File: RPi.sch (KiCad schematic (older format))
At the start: 8 parts, among them U3 LMS6002DR2, U4 ECP5, X3 RaspberryPiConnector

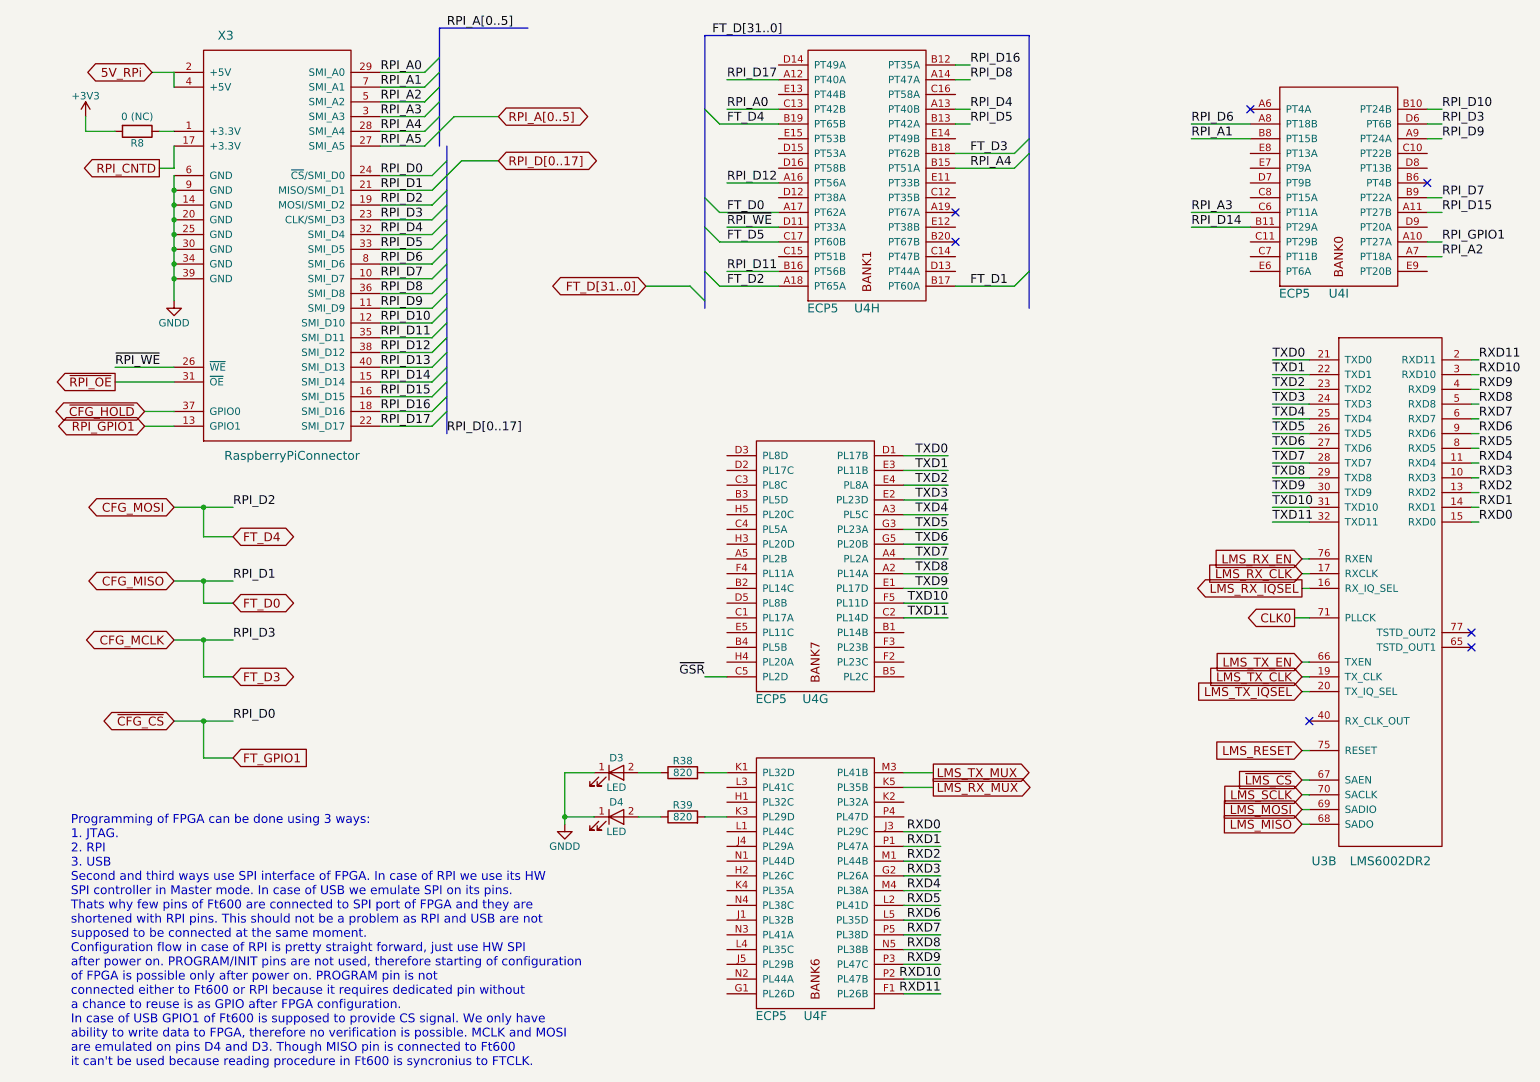
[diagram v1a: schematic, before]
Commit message: Start tracing IO Fix connector for Rpi Use LED indicator for TX/RX LEDs
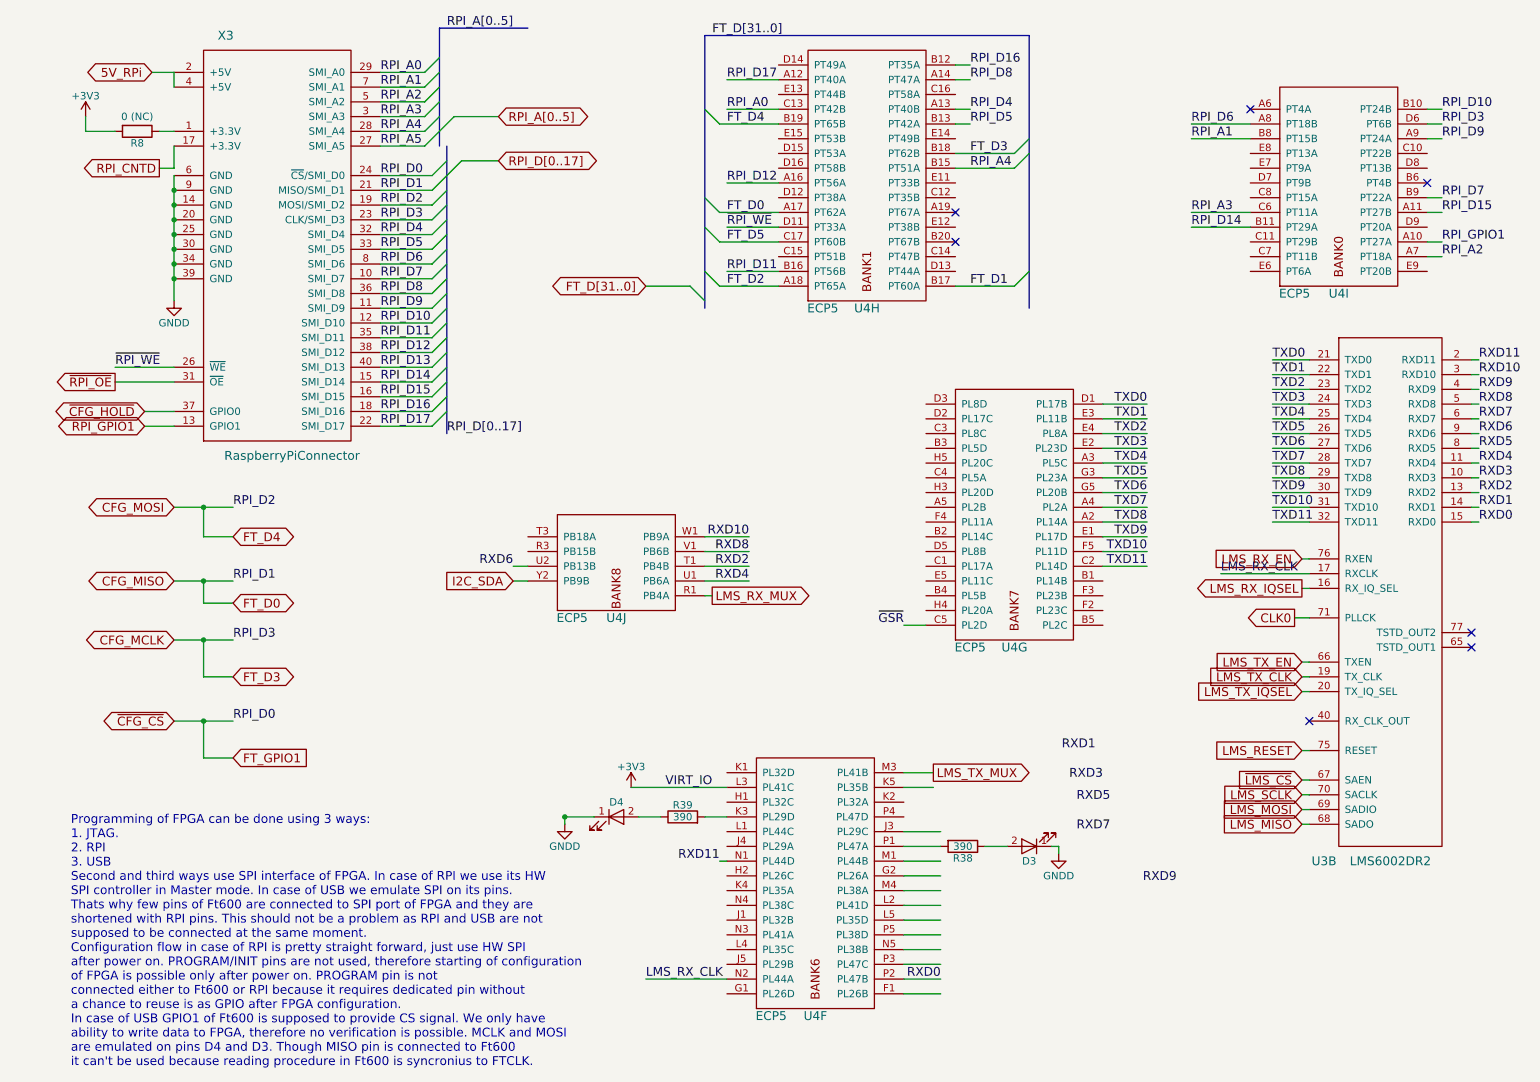
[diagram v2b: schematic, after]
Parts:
- added unit 10 of U4
- D3: value LED -> 5512509F; footprint (none) -> sdr-foots:LED_IND_SINGLE
- D4: value LED -> 5510209F; footprint (none) -> sdr-foots:LED_IND_SINGLE
- R38, R39: value 820 -> 390; footprint (none) -> Resistors_SMD:R_0603
- X3: footprint Pin_Headers:Pin_Header_Straight_2x20_Pitch2.54mm -> Socket_Strips:Socket_Strip_Straight_2x20_Pitch2.54mm
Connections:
- net labels added: I2C_SDA, VIRT_IO
- wire segments 148 -> 158
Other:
- moved on the sheet: D3, R38, U4G
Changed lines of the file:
@@
 $EndComp
 $Comp
-L +3V3 #PWR037
+L +3V3 #PWR039
 U 1 1 58A418F6
 P 800 1250
-F 0 "#PWR037" H 800 1100 50  0001 C CNN
+F 0 "#PWR039" H 800 1100 50  0001 C CNN
 F 1 "+3V3" H 800 1390 50  0000 C CNN
 F 2 "" H 800 1250 50  0000 C CNN
@@
 F 0 "X3" H 1750 6200 60  0000 C CNN
 F 1 "RaspberryPiConnector" H 2200 3350 60  0000 C CNN
-F 2 "Pin_Headers:Pin_Header_Straight_2x20_Pitch2.54mm" H 550 3850 60  0001 C CNN
+F 2 "Socket_Strips:Socket_Strip_Straight_2x20_Pitch2.54mm" H 550 3850 60  0001 C CNN
 F 3 "" H 550 3850 60  0001 C CNN
 	1    1600 3450
@@
 $EndComp
 $Comp
-L GNDD #PWR038
+L GNDD #PWR040
 U 1 1 58A80C0C
 P 1400 2500
-F 0 "#PWR038" H 1400 2250 50  0001 C CNN
+F 0 "#PWR040" H 1400 2250 50  0001 C CNN
 F 1 "GNDD" H 1400 2350 50  0000 C CNN
 F 2 "" H 1400 2500 50  0000 C CNN
@@
 	3350 1550 3600 1550
 Wire Wire Line
-	1800 3900 1400 3900
+	1400 3900 1800 3900
 Wire Wire Line
 	1400 4400 1800 4400
 Wire Wire Line
-	1800 4800 1400 4800
+	1400 4800 1800 4800
 Wire Wire Line
 	1400 5350 1800 5350
@@
 L ECP5 U4
 U 7 1 5924815B
-P 5350 5150
-F 0 "U4" H 5750 5100 60  0000 C CNN
-F 1 "ECP5" H 5450 5100 60  0000 C CNN
-F 2 "sdr-foots:ECP5_381" H 3800 5700 60  0001 C CNN
-F 3 "" H 3800 5700 60  0001 C CNN
-	7    5350 5150
+P 6700 4800
+F 0 "U4" H 7100 4750 60  0000 C CNN
+F 1 "ECP5" H 6800 4750 60  0000 C CNN
+F 2 "sdr-foots:ECP5_381" H 5150 5350 60  0001 C CNN
+F 3 "" H 5150 5350 60  0001 C CNN
+	7    6700 4800
 	1    0    0    -1
 $EndComp
 Text GLabel 6550 5700 2    60   Output ~ 0
 LMS_TX_MUX
-Text GLabel 6550 5800 2    60   Output ~ 0
+Text GLabel 5050 4500 2    60   Output ~ 0
 LMS_RX_MUX
 Wire Wire Line
 	6550 5700 6350 5700
-Text Label 6650 3550 2    60   ~ 0
+Text Label 8000 3200 2    60   ~ 0
 TXD0
-Text Label 6650 3650 2    60   ~ 0
+Text Label 8000 3300 2    60   ~ 0
 TXD1
-Text Label 6650 3750 2    60   ~ 0
+Text Label 8000 3400 2    60   ~ 0
 TXD2
-Text Label 6650 3850 2    60   ~ 0
+Text Label 8000 3500 2    60   ~ 0
 TXD3
-Text Label 6650 3950 2    60   ~ 0
+Text Label 8000 3600 2    60   ~ 0
 TXD4
-Text Label 6650 4050 2    60   ~ 0
+Text Label 8000 3700 2    60   ~ 0
 TXD5
-Text Label 6650 4150 2    60   ~ 0
+Text Label 8000 3800 2    60   ~ 0
 TXD6
-Text Label 6650 4250 2    60   ~ 0
+Text Label 8000 3900 2    60   ~ 0
 TXD7
-Text Label 6650 4350 2    60   ~ 0
+Text Label 8000 4000 2    60   ~ 0
 TXD8
-Text Label 6650 4450 2    60   ~ 0
+Text Label 8000 4100 2    60   ~ 0
 TXD9
-Text Label 6650 4550 2    60   ~ 0
+Text Label 8000 4200 2    60   ~ 0
 TXD10
-Text Label 6650 4650 2    60   ~ 0
+Text Label 8000 4300 2    60   ~ 0
 TXD11
 Wire Wire Line
-	6350 3550 6650 3550
-Wire Wire Line
-	6350 3650 6650 3650
-Wire Wire Line
-	6350 3750 6650 3750
-Wire Wire Line
-	6350 3850 6650 3850
-Wire Wire Line
-	6350 3950 6650 3950
-Wire Wire Line
-	6350 4050 6650 4050
-Wire Wire Line
-	6350 4150 6650 4150
-Wire Wire Line
-	6350 4250 6650 4250
-Wire Wire Line
-	6350 4350 6650 4350
-Wire Wire Line
-	6350 4450 6650 4450
-Wire Wire Line
-	6350 4550 6650 4550
-Wire Wire Line
-	6350 4650 6650 4650
-Text Label 6600 6100 2    60   ~ 0
+	7700 3200 8000 3200
+Wire Wire Line
+	7700 3300 8000 3300
+Wire Wire Line
+	7700 3400 8000 3400
+Wire Wire Line
+	7700 3500 8000 3500
+Wire Wire Line
+	7700 3600 8000 3600
+Wire Wire Line
+	7700 3700 8000 3700
+Wire Wire Line
+	7700 3800 8000 3800
+Wire Wire Line
+	7700 3900 8000 3900
+Wire Wire Line
+	7700 4000 8000 4000
+Wire Wire Line
+	7700 4100 8000 4100
+Wire Wire Line
+	7700 4200 8000 4200
+Wire Wire Line
+	7700 4300 8000 4300
+Text Label 6600 7100 2    60   ~ 0
 RXD0
-Text Label 6600 6200 2    60   ~ 0
+Text Label 7650 5550 2    60   ~ 0
 RXD1
-Text Label 6600 6300 2    60   ~ 0
+Text Label 5300 4300 2    60   ~ 0
 RXD2
-Text Label 6600 6400 2    60   ~ 0
+Text Label 7700 5750 2    60   ~ 0
 RXD3
-Text Label 6600 6500 2    60   ~ 0
+Text Label 5300 4400 2    60   ~ 0
 RXD4
-Text Label 6600 6600 2    60   ~ 0
+Text Label 7750 5900 2    60   ~ 0
 RXD5
-Text Label 6600 6700 2    60   ~ 0
+Text Label 3700 4300 2    60   ~ 0
 RXD6
-Text Label 6600 6800 2    60   ~ 0
+Text Label 7750 6100 2    60   ~ 0
 RXD7
-Text Label 6600 6900 2    60   ~ 0
+Text Label 5300 4200 2    60   ~ 0
 RXD8
-Text Label 6600 7000 2    60   ~ 0
+Text Label 8200 6450 2    60   ~ 0
 RXD9
-Text Label 6600 7100 2    60   ~ 0
+Text Label 5300 4100 2    60   ~ 0
 RXD10
-Text Label 6600 7200 2    60   ~ 0
+Text Label 5100 6300 2    60   ~ 0
 RXD11
 Wire Wire Line
@@
 Text GLabel 9050 4250 0    60   Input ~ 0
 LMS_RX_EN
-Text GLabel 9050 4350 0    60   Input ~ 0
-LMS_RX_CLK
 Text GLabel 9050 4450 0    60   Output ~ 0
 LMS_RX_IQSEL
@@
 	9100 4250 9050 4250
 Wire Wire Line
-	9050 4350 9100 4350
+	8500 4350 9100 4350
 Wire Wire Line
 	9100 4450 9050 4450
@@
 P 4400 6000
 F 0 "D4" H 4400 6100 50  0000 C CNN
-F 1 "LED" H 4400 5900 50  0000 C CNN
-F 2 "" H 4400 6000 50  0001 C CNN
+F 1 "5510209F" H 4400 5900 50  0001 C CNN
+F 2 "sdr-foots:LED_IND_SINGLE" H 4400 6000 50  0001 C CNN
 F 3 "" H 4400 6000 50  0001 C CNN
 	1    4400 6000
@@
 L LED D3
 U 1 1 5938F8CC
-P 4400 5700
-F 0 "D3" H 4400 5800 50  0000 C CNN
-F 1 "LED" H 4400 5600 50  0000 C CNN
-F 2 "" H 4400 5700 50  0001 C CNN
-F 3 "" H 4400 5700 50  0001 C CNN
-	1    4400 5700
-	1    0    0    -1
+P 7200 6200
+F 0 "D3" H 7200 6300 50  0000 C CNN
+F 1 "5512509F" H 7200 6100 50  0001 C CNN
+F 2 "sdr-foots:LED_IND_SINGLE" H 7200 6200 50  0001 C CNN
+F 3 "" H 7200 6200 50  0001 C CNN
+	1    7200 6200
+	-1   0    0    1
 $EndComp
 $Comp
 L R R38
 U 1 1 5938F9AA
-P 4850 5700
-F 0 "R38" V 4930 5700 50  0000 C CNN
-F 1 "820" V 4850 5700 50  0000 C CNN
-F 2 "" V 4780 5700 50  0001 C CNN
-F 3 "" H 4850 5700 50  0001 C CNN
-	1    4850 5700
-	0    -1   -1   0
+P 6750 6200
+F 0 "R38" V 6830 6200 50  0000 C CNN
+F 1 "390" V 6750 6200 50  0000 C CNN
+F 2 "Resistors_SMD:R_0603" V 6680 6200 50  0001 C CNN
+F 3 "" H 6750 6200 50  0001 C CNN
+	1    6750 6200
+	0    1    1    0
 $EndComp
 $Comp
@@
 P 4850 6000
 F 0 "R39" V 4930 6000 50  0000 C CNN
-F 1 "820" V 4850 6000 50  0000 C CNN
-F 2 "" V 4780 6000 50  0001 C CNN
+F 1 "390" V 4850 6000 50  0000 C CNN
+F 2 "Resistors_SMD:R_0603" V 4780 6000 50  0001 C CNN
 F 3 "" H 4850 6000 50  0001 C CNN
 	1    4850 6000
@@
 $EndComp
 Wire Wire Line
-	5150 5700 5000 5700
-Wire Wire Line
 	5000 6000 5150 6000
 Wire Wire Line
 	4700 6000 4550 6000
 Wire Wire Line
-	4700 5700 4550 5700
-$Comp
-L GNDD #PWR039
+	6900 6200 7050 6200
+$Comp
+L GNDD #PWR041
 U 1 1 5938FEB2
 P 4050 6050
-F 0 "#PWR039" H 4050 5800 50  0001 C CNN
+F 0 "#PWR041" H 4050 5800 50  0001 C CNN
 F 1 "GNDD" H 4050 5900 50  0000 C CNN
 F 2 "" H 4050 6050 50  0001 C CNN
@@
 	4250 6000 4050 6000
 Wire Wire Line
-	4050 5700 4050 6050
-Wire Wire Line
-	4250 5700 4050 5700
+	4050 6000 4050 6050
 Connection ~ 4050 6000
-Text Label 5000 5050 2    60   ~ 0
+Text Label 6350 4700 2    60   ~ 0
 ~GSR
 Wire Wire Line
-	5150 5050 5000 5050
+	6500 4700 6350 4700
+$Comp
+L ECP5 U4
+U 10 1 593A569C
+P 4000 4600
+F 0 "U4" H 4400 4550 60  0000 C CNN
+F 1 "ECP5" H 4100 4550 60  0000 C CNN
+F 2 "sdr-foots:ECP5_381" H 2450 5150 60  0001 C CNN
+F 3 "" H 2450 5150 60  0001 C CNN
+	10   4000 4600
+	1    0    0    -1
+$EndComp
+Wire Wire Line
+	5300 4200 5000 4200
+Wire Wire Line
+	5300 4100 5000 4100
+Text GLabel 3700 4400 0    60   Input ~ 0
+I2C_SDA
+Wire Wire Line
+	3800 4400 3700 4400
+Wire Wire Line
+	5300 4400 5000 4400
+Wire Wire Line
+	3800 4300 3700 4300
+Wire Wire Line
+	5300 4300 5000 4300
+Text Label 8500 4350 0    60   ~ 0
+LMS_RX_CLK
+Text Label 4600 7100 0    60   ~ 0
+LMS_RX_CLK
+Wire Wire Line
+	5150 7100 4600 7100
+Wire Wire Line
+	5050 4500 5000 4500
+$Comp
+L GNDD #PWR042
+U 1 1 593A9507
+P 7400 6250
+F 0 "#PWR042" H 7400 6000 50  0001 C CNN
+F 1 "GNDD" H 7400 6100 50  0000 C CNN
+F 2 "" H 7400 6250 50  0001 C CNN
+F 3 "" H 7400 6250 50  0001 C CNN
+	1    7400 6250
+	1    0    0    -1
+$EndComp
+Wire Wire Line
+	7400 6250 7400 6200
+Wire Wire Line
+	7400 6200 7350 6200
+$Comp
+L +3V3 #PWR043
+U 1 1 593A9CC5
+P 4500 5800
+F 0 "#PWR043" H 4500 5650 50  0001 C CNN
+F 1 "+3V3" H 4500 5940 50  0000 C CNN
+F 2 "" H 4500 5800 50  0000 C CNN
+F 3 "" H 4500 5800 50  0000 C CNN
+	1    4500 5800
+	1    0    0    -1
+$EndComp
+Wire Wire Line
+	5150 5800 4500 5800
+Text Label 5050 5800 2    60   ~ 0
+VIRT_IO
+Wire Wire Line
+	5150 6300 5100 6300
 $EndSCHEMATC

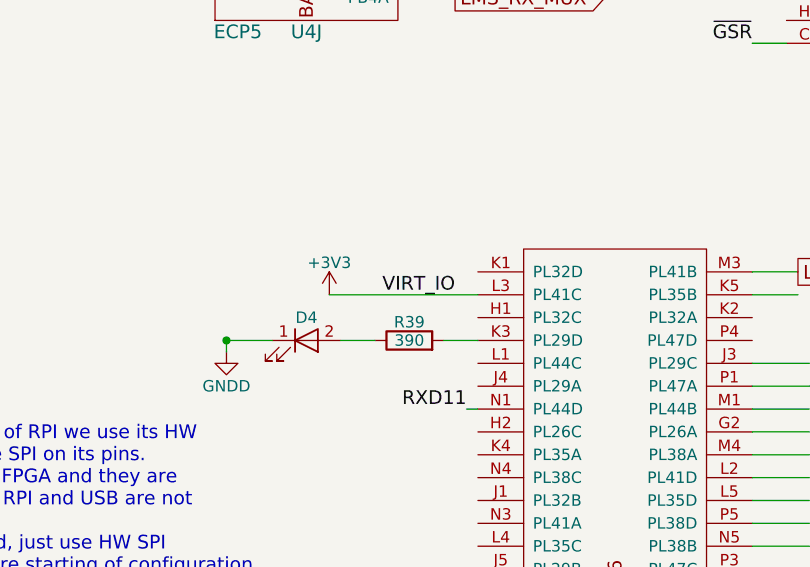
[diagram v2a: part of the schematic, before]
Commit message: Add VCCIO and some vias
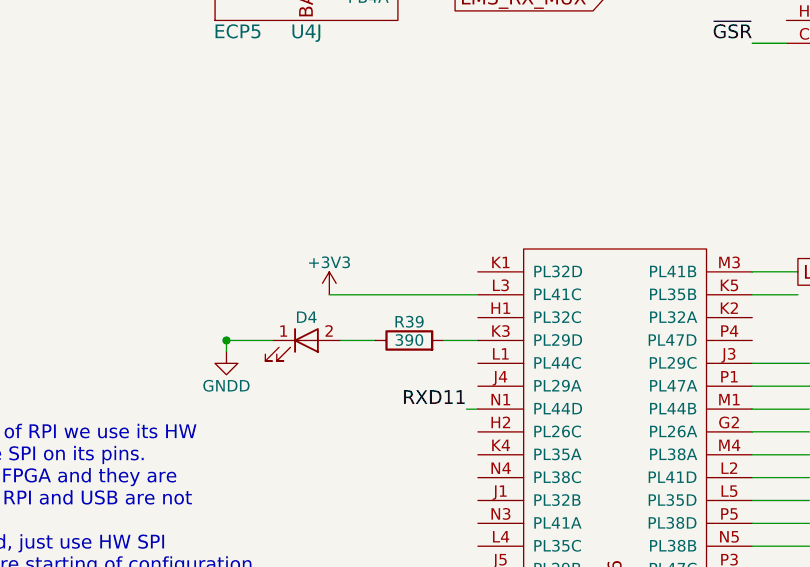
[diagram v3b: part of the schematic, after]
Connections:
- net labels removed: VIRT_IO
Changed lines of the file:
@@
 Wire Wire Line
 	5150 5800 4500 5800
-Text Label 5050 5800 2    60   ~ 0
-VIRT_IO
 Wire Wire Line
 	5150 6300 5100 6300
